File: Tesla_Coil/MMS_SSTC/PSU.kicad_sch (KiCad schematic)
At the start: 3 parts, among them U6 TL494IN, U7 TL071CP

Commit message: Commit additions to SSTC PSU schematic
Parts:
- added C20: 3.3u, Capacitor_THT:C_Rect_L31.5mm_W17.0mm_P27.50mm_MKS4, symbol Device:C_Small
- added C21, C23: 470u, Capacitor_THT:CP_Radial_D12.5mm_P5.00mm, symbol Device:C_Polarized_Small
- added C22, C24, C25: 0.1u, Capacitor_THT:C_Disc_D3.0mm_W2.0mm_P2.50mm, symbol Device:C_Small
- added C26: C_Small, symbol Device:C_Small
- added D10: 20V 3W, symbol Device:D_Zener
- added D11, D9: D_Bridge_+-AA, symbol Device:D_Bridge_+-AA
- added Q2: IRF740, Package_TO_SOT_THT:TO-220-3_Vertical, symbol Transistor_FET:IRF740
- added R10, R11, R6, R7, R8, R9: R_Small_US, symbol Device:R_Small_US
- added R4: R_US, symbol Device:R_US
- added U10: IR2011, symbol Driver_FET:IR2011
- added U8: LM7812_TO220, Package_TO_SOT_THT:TO-220-3_Vertical, symbol Regulator_Linear:LM7812_TO220
- added U9: LM7805_TO220, Package_TO_SOT_THT:TO-220-3_Vertical, symbol Regulator_Linear:LM7805_TO220
- U7: DKPN (none) -> 296-7186-5-ND
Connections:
- net at L2.1: now also Q2.3 (S)
- net at L2.2: now also R4.1, R7.1
- new net: R10.1, R7.2, R8.2
- new net: R11.1, R6.2, R9.1
- new net: C21.1, C22.1, D10.1 (K), D9.1 (+), U8.1 (VI)
- new net: C20.2, D9.3
- new net: R4.2, R6.1
- new net: C26.1, D11.1 (+), Q2.2 (D)
- new net +12V: C23.1, C24.1, U8.3 (VO), U9.1 (VI)
- new net +5V: C25.1, U9.3 (VO)
- new net GND: C21.2, C22.2, C23.2, C24.2, C25.2, C26.2, D10.2 (A), D11.2 (-), D9.2 (-), R8.1, R9.2, U8.2 (GND), U9.2 (GND)
- new net HT: C20.1, D11.3
- new net NEUT: D11.4, D9.4
- no-connect marks 2 -> 0
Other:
- note added: "15v zener also viable"
- note added: "3.3u is probably oversize, I can likely get away with 1.5u. Need to more closely measure logic cct to get power usage."
- note added: "IR2118PBF-ND like might work but itll add 0.3us propogation to the fet actually switching"
- note added: "NOT EARTH GROUND!"
- note added: "i think this is for high and low side, not high or low side i might have to use a different gd"
- moved on the sheet: L2, U6, U7

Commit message: Begin work on final tesla coil design
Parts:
- removed C20: 3.3u, Capacitor_THT:C_Rect_L31.5mm_W17.0mm_P27.50mm_MKS4, symbol Device:C_Small
- removed C21, C23: 470u, Capacitor_THT:CP_Radial_D12.5mm_P5.00mm, symbol Device:C_Polarized_Small
- removed C22, C24, C25: 0.1u, Capacitor_THT:C_Disc_D3.0mm_W2.0mm_P2.50mm, symbol Device:C_Small
- removed C26: C_Small, symbol Device:C_Small
- removed D10: 20V 3W, symbol Device:D_Zener
- removed D11, D9: D_Bridge_+-AA, symbol Device:D_Bridge_+-AA
- removed L2: 100u, Inductor_THT:L_Radial_D21.0mm_P19.00mm, symbol Device:L_Ferrite
- removed Q2: IRF740, Package_TO_SOT_THT:TO-220-3_Vertical, symbol Transistor_FET:IRF740
- removed R10, R11, R6, R7, R8, R9: R_Small_US, symbol Device:R_Small_US
- removed R4: R_US, symbol Device:R_US
- removed U10: IR2011, symbol Driver_FET:IR2011
- removed U6: TL494IN, Package_DIP:DIP-16_W7.62mm, symbol locals:TL494IN
- removed U7: TL071CP, Package_DIP:DIP-8_W7.62mm, symbol locals:TL071CP
- removed U8: LM7812_TO220, Package_TO_SOT_THT:TO-220-3_Vertical, symbol Regulator_Linear:LM7812_TO220
- removed U9: LM7805_TO220, Package_TO_SOT_THT:TO-220-3_Vertical, symbol Regulator_Linear:LM7805_TO220
- added C1, C3: 470u, Capacitor_THT:CP_Radial_D12.5mm_P5.00mm, symbol Device:C_Polarized_Small
- added C2, C4, C5, C7: 0.1u, Capacitor_THT:C_Disc_D3.0mm_W2.0mm_P2.50mm, symbol Device:C_Small
- added C6: 1500u, Capacitor_THT:CP_Radial_D30.0mm_P10.00mm_SnapIn, symbol Device:C_Polarized_Small
- added C8: 1u, Capacitor_THT:C_Rect_L18.0mm_W7.0mm_P15.00mm_FKS3_FKP3, symbol Device:C_Small
- added D1: D_Filled, Diode_THT:D_DO-41_SOD81_P7.62mm_Horizontal, symbol Device:D_Filled
- added D2: B125C2300-1500A, Diode_THT:Diode_Bridge_Vishay_GBU, symbol Diode_Bridge:B125C2300-1500A
- added J1: Screw_Terminal_01x02, locals:691137710003, symbol Connector:Screw_Terminal_01x03
- added R2: 18k, Resistor_THT:R_Axial_DIN0617_L17.0mm_D6.0mm_P5.08mm_Vertical, symbol Device:R_Small_US
- added TR2: TRANSF1, symbol Transformer:TRANSF1
- added U1: LM7812_TO220, Package_TO_SOT_THT:TO-220-3_Vertical, symbol Regulator_Linear:LM7812_TO220
- added U2: LM7805_TO220, Package_TO_SOT_THT:TO-220-3_Vertical, symbol Regulator_Linear:LM7805_TO220
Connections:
- net +12V: now also C3.1, C4.1, C7.1, U1.3 (VO), U2.1 (VI)
- net +5V: now also C5.1, U2.3 (VO)
- net GND: now also C1.2, C2.2, C3.2, C4.2, C5.2, C6.2, C7.2, C8.2, D2.1 (-), R2.2, TR2.3, U1.2 (GND), U2.2 (GND)
- net HT: now also D2.2, J1.1 (Pin_1), TR2.1
- net NEUT: now also D2.3, J1.2 (Pin_2), TR2.2
- new net: C1.1, C2.1, D1.1 (K), U1.1 (VI)
- new net +170V: C6.1, C8.1, D2.4 (+), R2.1
- new net 24VAC: D1.2 (A), TR2.4
- new net Earth: J1.3 (Pin_3)
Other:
- note added: "Both caps rated to 200v note this in whatever nice final printout"
- note added: "NOT earth ground!!!!"
- note added: "bleeder is high power 3 watt want fast discharge for curious people"
- note added: "in final schematic printout if this is ever published we need to have a couple warnings about stuff like grounding because this design ideally is NOT isolated"
- note added: "might be good to add attachement points for aux DC if doing testing at lower voltages where the transformer may not supply necessary power"
- note added: "power switch and fuse still needed"
- note removed: "15v zener also viable"
- note removed: "3.3u is probably oversize, I can likely get away with 1.5u. Need to more closely measure logic cct to get power usage."
- note removed: "IR2118PBF-ND like might work but itll add 0.3us propogation to the fet actually switching"
- note removed: "NOT EARTH GROUND!"
- note removed: "i think this is for high and low side, not high or low side i might have to use a different gd"

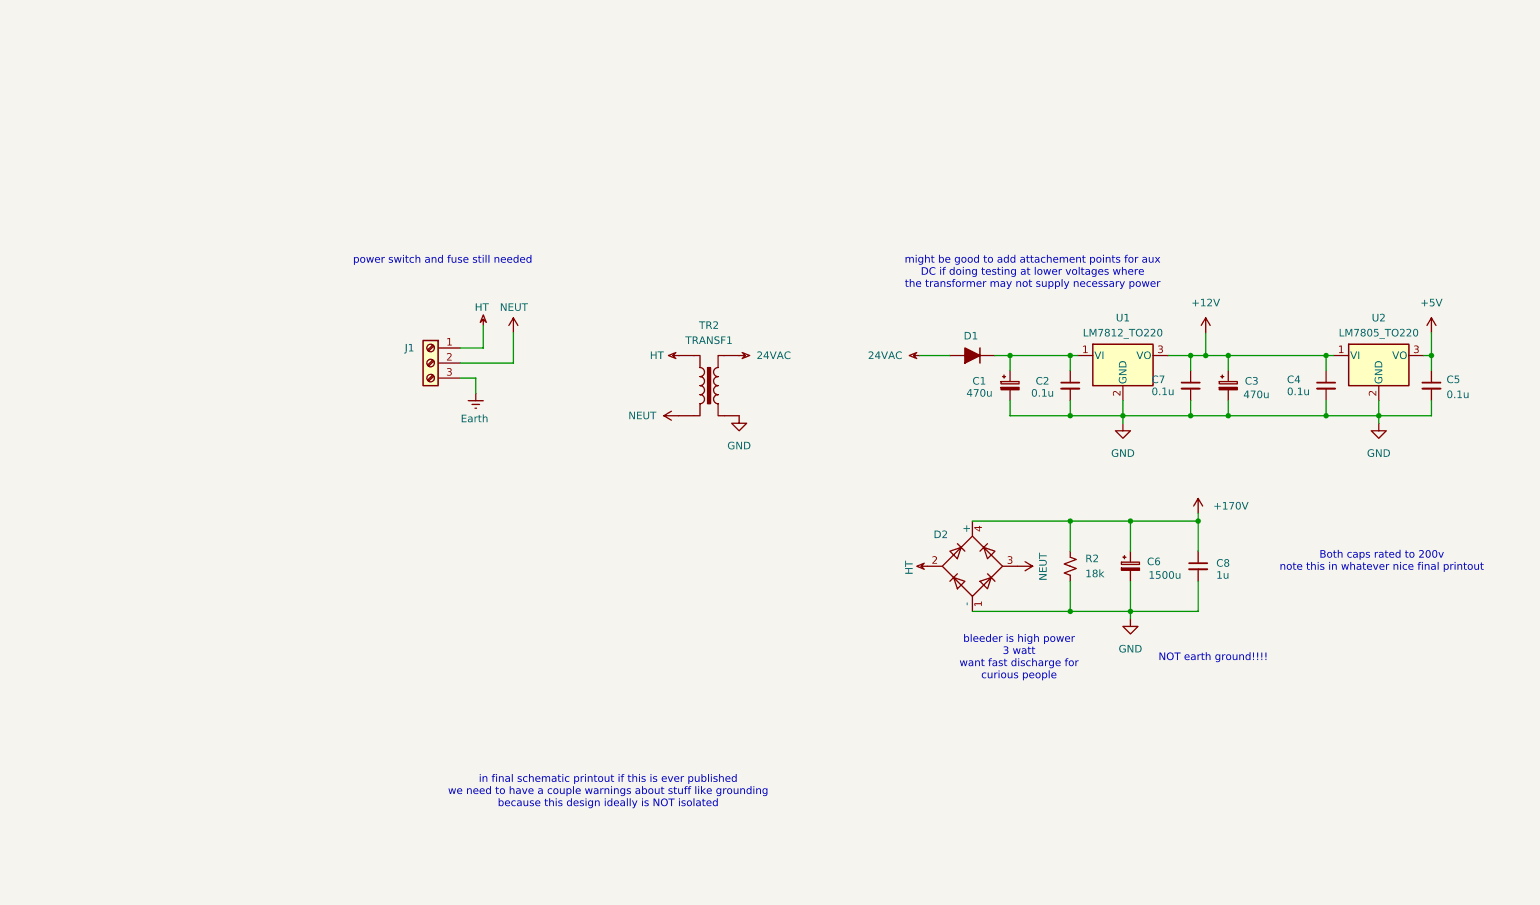
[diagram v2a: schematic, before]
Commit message: Add changes to tesla coil schematic and coil winder parts
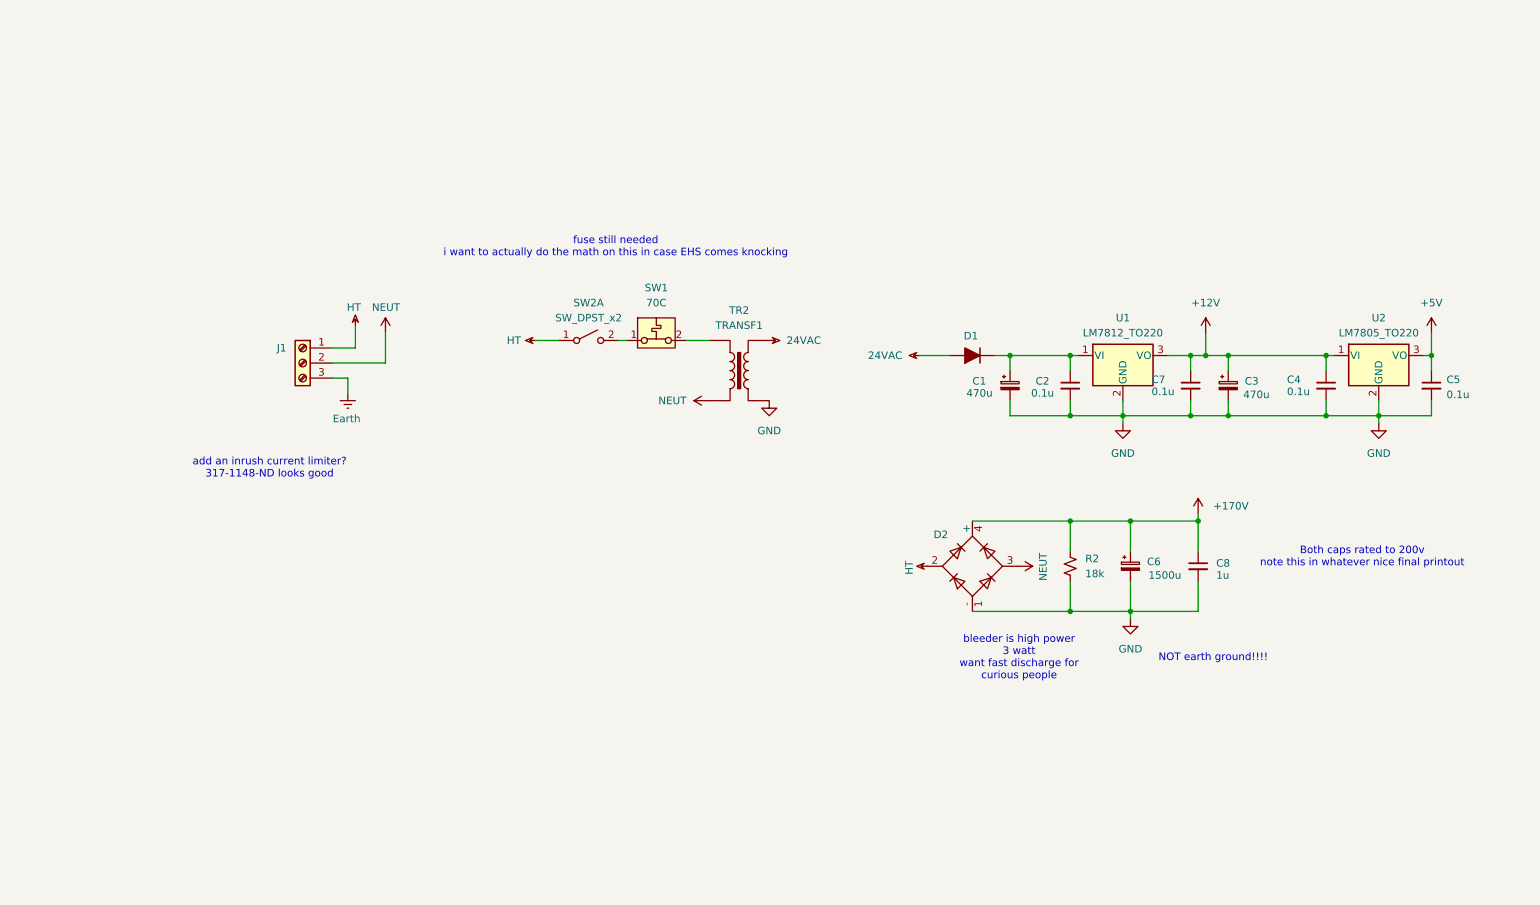
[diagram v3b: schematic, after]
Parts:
- added SW1: 70C, Package_TO_SOT_THT:TO-220-2_Vertical, symbol Switch:SW_SPST_Temperature
- added SW2: SW_DPST_x2, symbol Switch:SW_DPST_x2
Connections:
- net HT: now also SW2.1 (A); no longer TR2.1
- new net: SW1.1 (A), SW2.2 (B)
- new net: SW1.2 (B), TR2.1
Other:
- note added: "add an inrush current limiter? 317-1148-ND looks good"
- note added: "fuse still needed i want to actually do the math on this in case EHS comes knocking"
- note removed: "in final schematic printout if this is ever published we need to have a couple warnings about stuff like grounding because this design ideally is NOT isolated"
- note removed: "might be good to add attachement points for aux DC if doing testing at lower voltages where the transformer may not supply necessary power"
- note removed: "power switch and fuse still needed"
- moved on the sheet: J1, TR2

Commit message: Draft BOM for final SSTC design
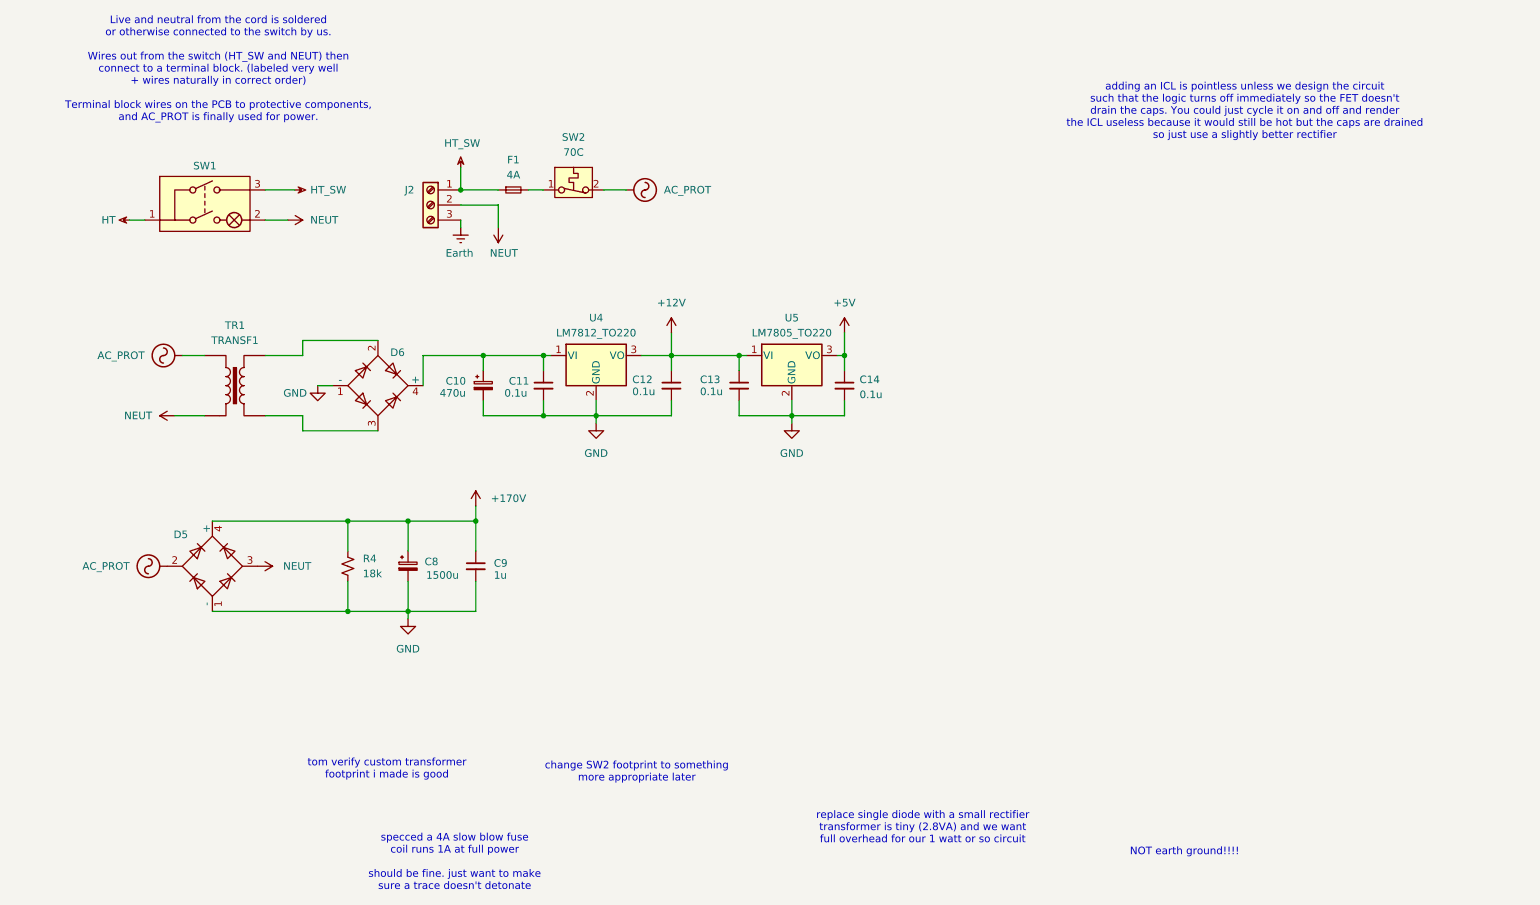
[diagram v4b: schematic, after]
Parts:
- removed C3: 470u, Capacitor_THT:CP_Radial_D12.5mm_P5.00mm, symbol Device:C_Polarized_Small
- removed D1: D_Filled, Diode_THT:D_DO-41_SOD81_P7.62mm_Horizontal, symbol Device:D_Filled
- removed SW2: SW_DPST_x2, symbol Switch:SW_DPST_x2
- added D6: DB105, Diode_THT:Diode_Bridge_DIP-4_W7.62mm_P5.08mm, symbol Diode_Bridge:B125C2300-1500A
- added F1: 4A, Resistor_THT:R_Axial_DIN0411_L9.9mm_D3.6mm_P12.70mm_Horizontal, symbol Device:Fuse_Small
- added SW1: SW_Rocker_3_Prong_Illuminated, symbol locals:SW_Rocker_3_Prong_Illuminated
- TR1: renamed from TR2; footprint (none) -> locals:Transformer_Zettler_BV301S18028; DKPN 3388-BV301S24028-ND -> 3388-BV301S18028-ND
- renumbered C1 to C10, C2 to C11, C7 to C12, C4 to C13, C5 to C14, C6 to C8, C8 to C9, D2 to D5, J1 to J2, R2 to R4, SW1 to SW2, U1 to U4, U2 to U5
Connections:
- net GND: now also D6.1 (-); no longer TR1.3
- net HT: now also SW1.1; no longer D5.2, J2.1 (Pin_1)
- net NEUT: now also SW1.2
- net at SW2.1 (A): now also F1.2
- net AC_PROT: now reaches SW2.2 (B), TR1.1
- net AC_PROT: now also D5.2
- net at C10.1, C11.1, U4.1 (VI): now also D6.4 (+)
- net 24VAC: no longer names the net of TR1.4
- net 24VAC: now also D6.2
- new net: D6.3, TR1.3
- new net HT_SW: F1.1, J2.1 (Pin_1), SW1.3
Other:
- note added: "Live and neutral from the cord is soldered or otherwise connected to the switch by us. Wires out from the switch (HT_SW and NEUT) then connect to a terminal block. (labeled very well + wires naturally in correct order) Terminal block wires on the PCB to protective components, and AC_PROT is finally used for power."
- note added: "adding an ICL is pointless unless we design the circuit such that the logic turns off immediately so the FET doesn't drain the caps. You could just cycle it on and off and render the ICL useless because it would still be hot but the caps are drained so just use a slightly better rectifier"
- note added: "change SW2 footprint to something more appropriate later"
- note added: "replace single diode with a small rectifier transformer is tiny (2.8VA) and we want full overhead for our 1 watt or so circuit"
- note added: "specced a 4A slow blow fuse coil runs 1A at full power should be fine. just want to make sure a trace doesn't detonate"
- note added: "tom verify custom transformer footprint i made is good"
- note removed: "Both caps rated to 200v note this in whatever nice final printout"
- note removed: "add an inrush current limiter? 317-1148-ND looks good"
- note removed: "bleeder is high power 3 watt want fast discharge for curious people"
- note removed: "fuse still needed i want to actually do the math on this in case EHS comes knocking"
- moved on the sheet: C10, C11, C12, C13, C14, C8, C9, D5, J2, R4, SW2, TR1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

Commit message: apply cost saving measures
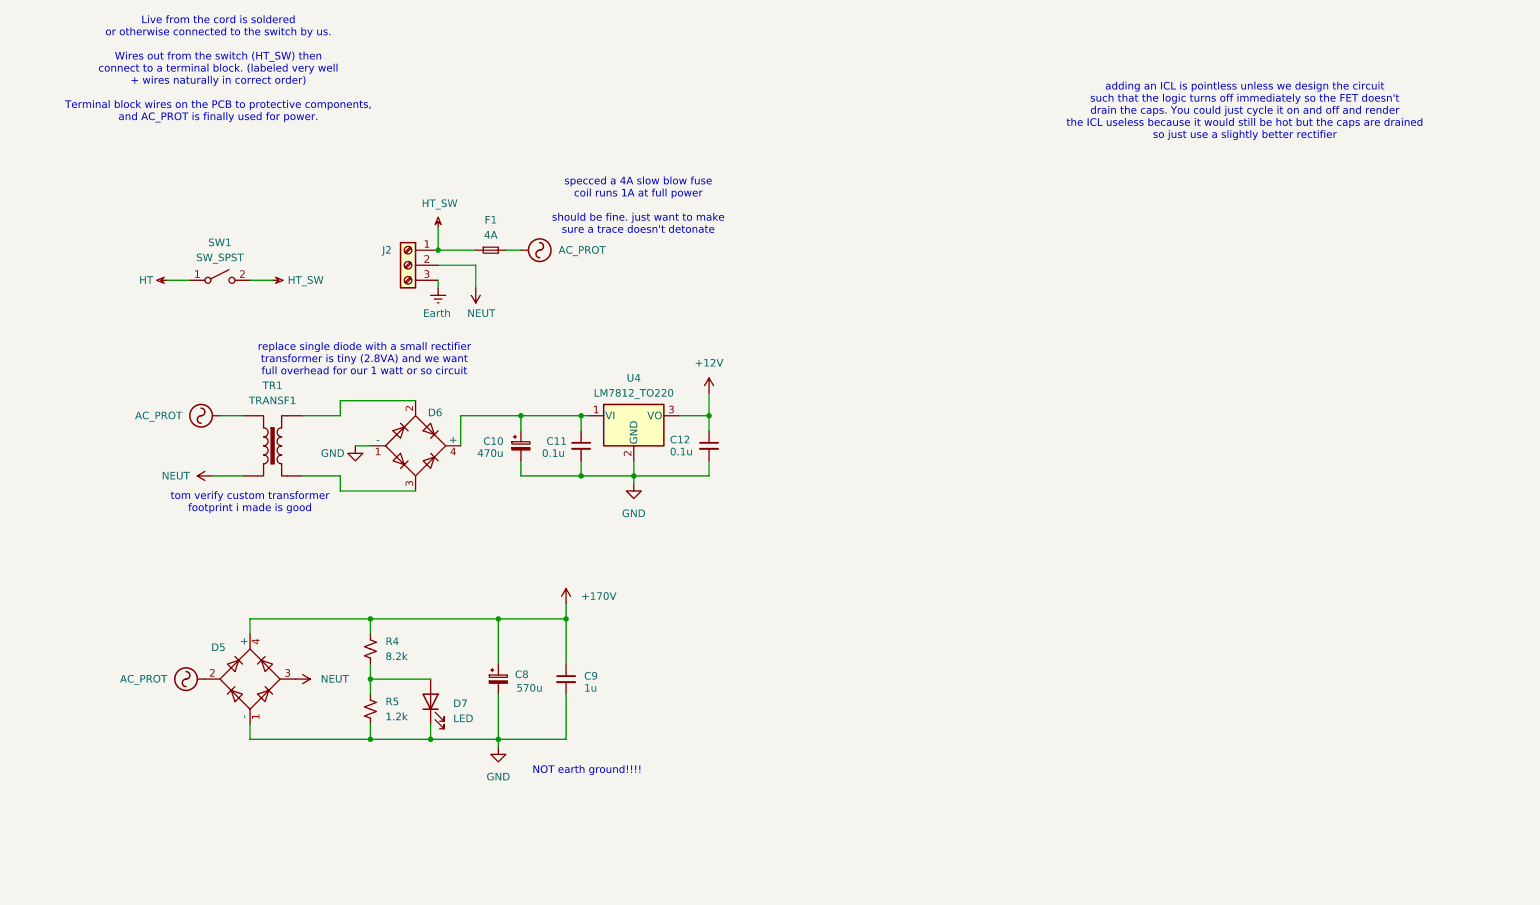
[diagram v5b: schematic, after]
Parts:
- removed C13, C14: 0.1u, Capacitor_THT:C_Disc_D3.0mm_W2.0mm_P2.50mm, symbol Device:C_Small
- removed SW1: SW_Rocker_3_Prong_Illuminated, symbol locals:SW_Rocker_3_Prong_Illuminated
- removed SW2: 70C, Package_TO_SOT_THT:TO-220-2_Vertical, symbol Switch:SW_SPST_Temperature
- removed U5: LM7805_TO220, Package_TO_SOT_THT:TO-220-3_Vertical, symbol Regulator_Linear:LM7805_TO220
- added D7: LED, LED_THT:LED_D3.0mm_Horizontal_O1.27mm_Z2.0mm, symbol Device:LED
- added R5: 1.2k, Resistor_THT:R_Axial_DIN0204_L3.6mm_D1.6mm_P5.08mm_Horizontal, symbol Device:R_Small_US
- added SW1: SW_SPST, symbol Switch:SW_SPST
- C8: value 1500u -> 570u; DKPN 565-3693-ND -> 565-2951-ND
- R4: value 18k -> 8.2k; DKPN RSF2JT18K0CT-ND -> A142822CT-ND
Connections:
- net AC_PROT: now also F1.2
- net GND: now also D7.1 (K), R5.2; no longer R4.2
- net HT: now also SW1.1 (A)
- net HT_SW: now also SW1.2 (B)
- new net: D7.2 (A), R4.2, R5.1
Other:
- note added: "Live from the cord is soldered or otherwise connected to the switch by us. Wires out from the switch (HT_SW) then connect to a terminal block. (labeled very well + wires naturally in correct order) Terminal block wires on the PCB to protective components, and AC_PROT is finally used for power."
- note removed: "Live and neutral from the cord is soldered or otherwise connected to the switch by us. Wires out from the switch (HT_SW and NEUT) then connect to a terminal block. (labeled very well + wires naturally in correct order) Terminal block wires on the PCB to protective components, and AC_PROT is finally used for power."
- note removed: "change SW2 footprint to something more appropriate later"
- moved on the sheet: C10, C11, C12, C8, C9, D5, D6, F1, J2, R4, TR1, U4
